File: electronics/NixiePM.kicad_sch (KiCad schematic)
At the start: 15 parts, among them U1 IRM-03-5, U2 16A 20mm 500V 5mm Plugin Fuse, U3 ESP32-ZERO, U4 QNHC3, U5 74HC595D,118, U6 74HC595D,118, U7 74HC595D,118, U8 KAQY214ATLD

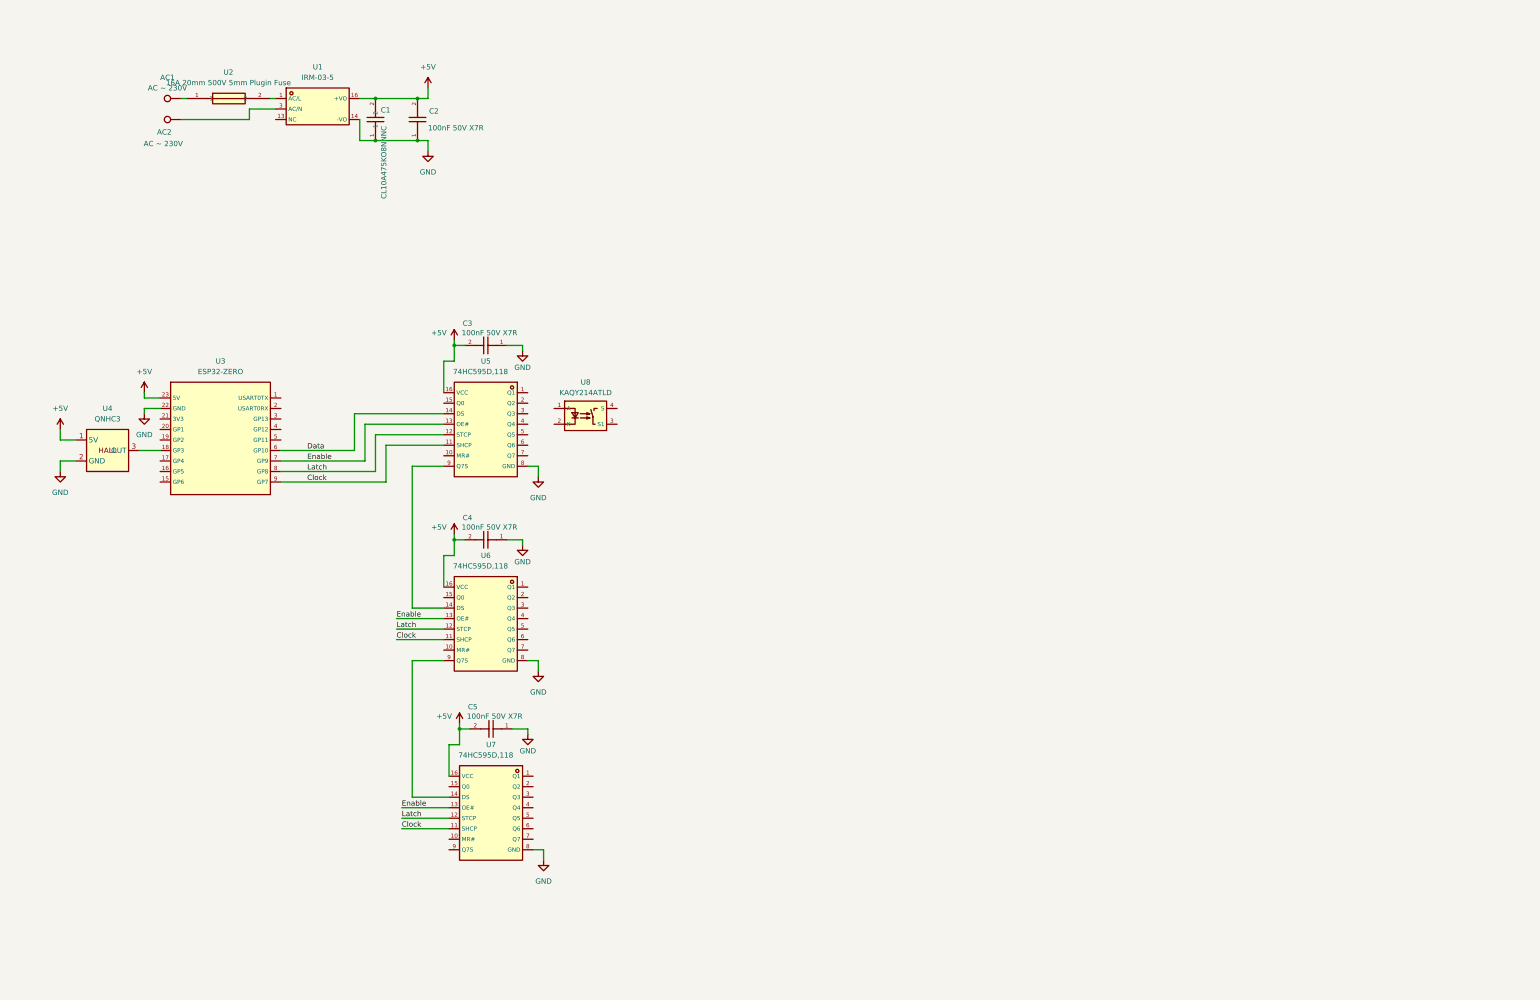
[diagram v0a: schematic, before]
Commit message: schematic ready, layout started
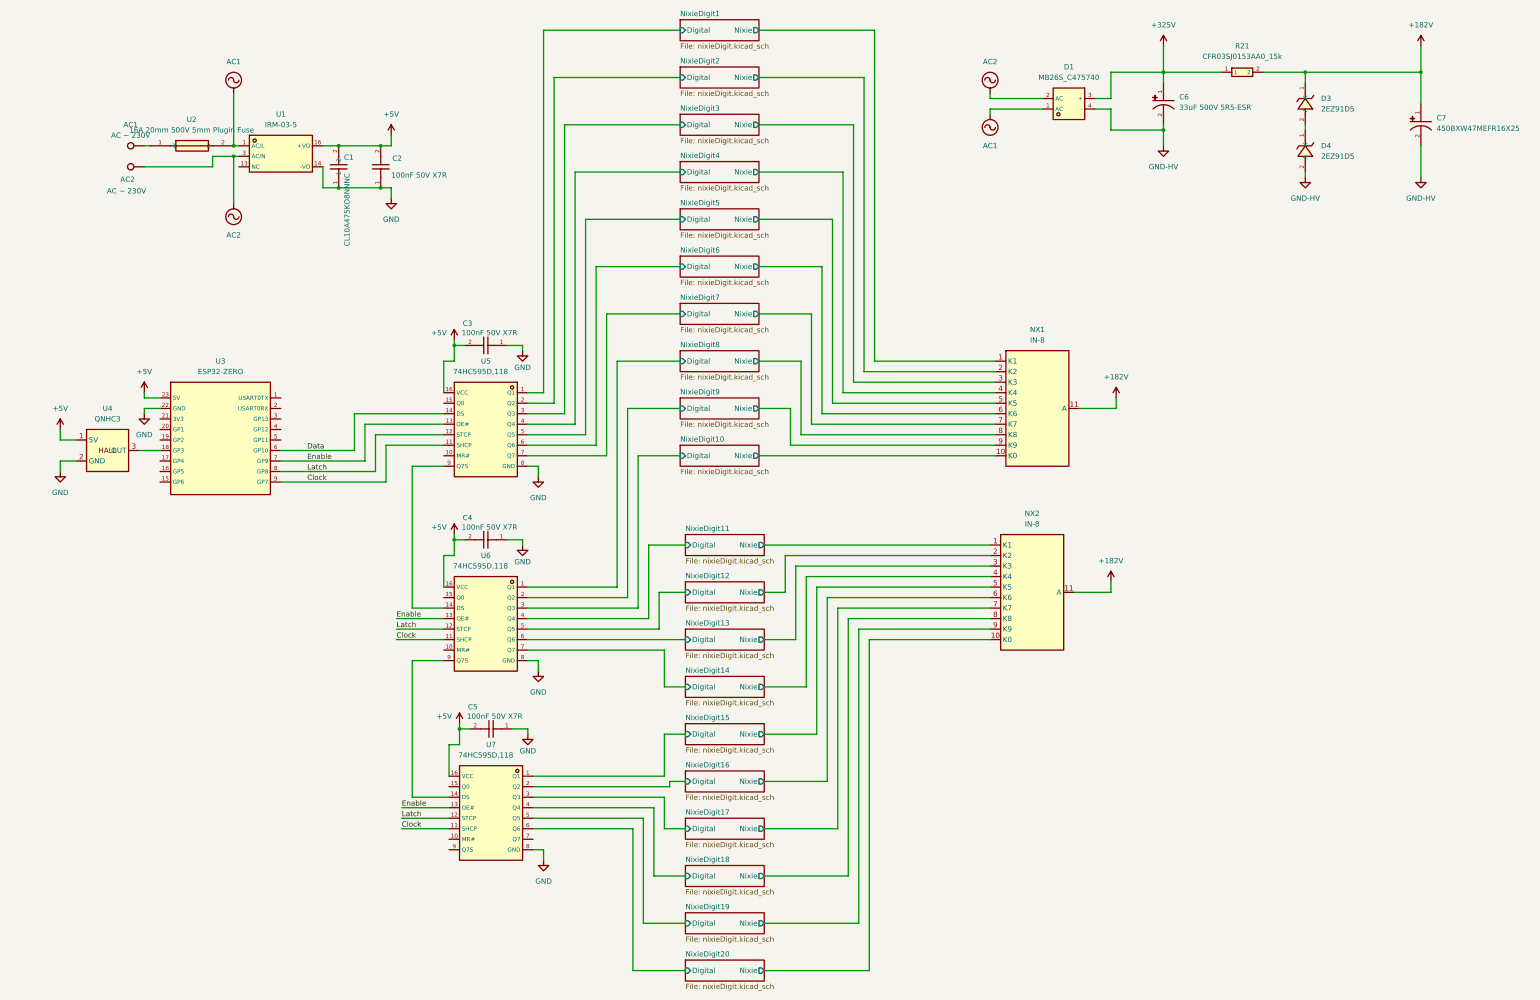
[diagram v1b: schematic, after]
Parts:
- removed U8: KAQY214ATLD, footprints:SMD-4_L4.6-W6.4-P2.54-LS10.0-BR, symbol symbols:KAQY214ATLD
- added C6: 33uF 500V 5R5-ESR, footprints:CAP-TH_BD12.5-P5.00-D0.6-FD, symbol symbols:LKML2502H330MF
- added C7: 450BXW47MEFR16X25, footprints:CAP-TH_BD16.0-P7.50-D1.2-FD, symbol symbols:450BXW47MEFR16X25
- added D1: MB26S_C475740, footprints:MBS_L4.7-W4.0-P2.50-LS7.0-BL, symbol symbols:MB26S_C475740
- added D3, D4: 2EZ91D5, footprints:DO-41_BD2.4-L4.7-P8.70-D0.8-RD, symbol symbols:2EZ91D5
- added NX1, NX2: IN-8, footprints:IN-8_NIXIE, symbol symbols:IN-8
- added R21: CFR03SJ0153AA0_15k, footprints:RES-TH_BD6.0-L17.5-P21.50-D0.8, symbol symbols:CFR03SJ0153AA0
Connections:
- net NixieDigit1/Digital: now reaches U5.1 (Q1)
- net NixieDigit2/Digital: now reaches U5.2 (Q2)
- net NixieDigit3/Digital: now reaches U5.3 (Q3)
- net NixieDigit4/Digital: now reaches U5.4 (Q4)
- net NixieDigit5/Digital: now reaches U5.5 (Q5)
- net NixieDigit6/Digital: now reaches U5.6 (Q6)
- net NixieDigit7/Digital: now reaches U5.7 (Q7)
- net AC2: now reaches AC2.1, U1.3 (AC/N)
- net AC2: now also D1.2 (AC)
- net NixieDigit8/Digital: now reaches U6.1 (Q1)
- net NixieDigit9/Digital: now reaches U6.2 (Q2)
- net NixieDigit10/Digital: now reaches U6.3 (Q3)
- net NixieDigit11/Digital: now reaches U6.4 (Q4)
- net NixieDigit12/Digital: now reaches U6.5 (Q5)
- net NixieDigit13/Digital: now reaches U6.6 (Q6)
- net NixieDigit14/Digital: now reaches U6.7 (Q7)
- net AC1: now reaches U1.1 (AC/L), U2.2
- net AC1: now also D1.1 (AC)
- net NixieDigit15/Digital: now reaches U7.1 (Q1)
- net NixieDigit16/Digital: now reaches U7.2 (Q2)
- net NixieDigit17/Digital: now reaches U7.3 (Q3)
- net NixieDigit18/Digital: now reaches U7.4 (Q4)
- net NixieDigit19/Digital: now reaches U7.5 (Q5)
- net NixieDigit20/Digital: now reaches U7.6 (Q6)
- new net: D3.2 (A), D4.1 (K)
- new net +182V: C7.1, D3.1 (K), NX1.11 (A), NX2.11 (A), R21.2
- new net +325V: C6.1, D1.3 (+), R21.1
- new net GND-HV: C6.2, C7.2, D1.4 (-), D4.2 (A)
- new net NixieDigit1/Nixie: NX1.1 (K1)
- new net NixieDigit10/Nixie: NX1.10 (K0)
- new net NixieDigit11/Nixie: NX2.1 (K1)
- new net NixieDigit12/Nixie: NX2.2 (K2)
- new net NixieDigit13/Nixie: NX2.3 (K3)
- new net NixieDigit14/Nixie: NX2.4 (K4)
- new net NixieDigit15/Nixie: NX2.5 (K5)
- new net NixieDigit16/Nixie: NX2.6 (K6)
- new net NixieDigit17/Nixie: NX2.7 (K7)
- new net NixieDigit18/Nixie: NX2.8 (K8)
- new net NixieDigit19/Nixie: NX2.9 (K9)
- new net NixieDigit2/Nixie: NX1.2 (K2)
- new net NixieDigit20/Nixie: NX2.10 (K0)
- new net NixieDigit3/Nixie: NX1.3 (K3)
- new net NixieDigit4/Nixie: NX1.4 (K4)
- new net NixieDigit5/Nixie: NX1.5 (K5)
- new net NixieDigit6/Nixie: NX1.6 (K6)
- new net NixieDigit7/Nixie: NX1.7 (K7)
- new net NixieDigit8/Nixie: NX1.8 (K8)
- new net NixieDigit9/Nixie: NX1.9 (K9)
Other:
- added sheet NixieDigit1 (nixieDigit.kicad_sch)
- added sheet NixieDigit10 (nixieDigit.kicad_sch)
- added sheet NixieDigit11 (nixieDigit.kicad_sch)
- added sheet NixieDigit12 (nixieDigit.kicad_sch)
- added sheet NixieDigit13 (nixieDigit.kicad_sch)
- added sheet NixieDigit14 (nixieDigit.kicad_sch)
- added sheet NixieDigit15 (nixieDigit.kicad_sch)
- added sheet NixieDigit16 (nixieDigit.kicad_sch)
- added sheet NixieDigit17 (nixieDigit.kicad_sch)
- added sheet NixieDigit18 (nixieDigit.kicad_sch)
- added sheet NixieDigit19 (nixieDigit.kicad_sch)
- added sheet NixieDigit2 (nixieDigit.kicad_sch)
- added sheet NixieDigit20 (nixieDigit.kicad_sch)
- added sheet NixieDigit3 (nixieDigit.kicad_sch)
- added sheet NixieDigit4 (nixieDigit.kicad_sch)
- added sheet NixieDigit5 (nixieDigit.kicad_sch)
- added sheet NixieDigit6 (nixieDigit.kicad_sch)
- added sheet NixieDigit7 (nixieDigit.kicad_sch)
- added sheet NixieDigit8 (nixieDigit.kicad_sch)
- added sheet NixieDigit9 (nixieDigit.kicad_sch)
- moved on the sheet: AC1, AC2, C1, C2, U1, U2

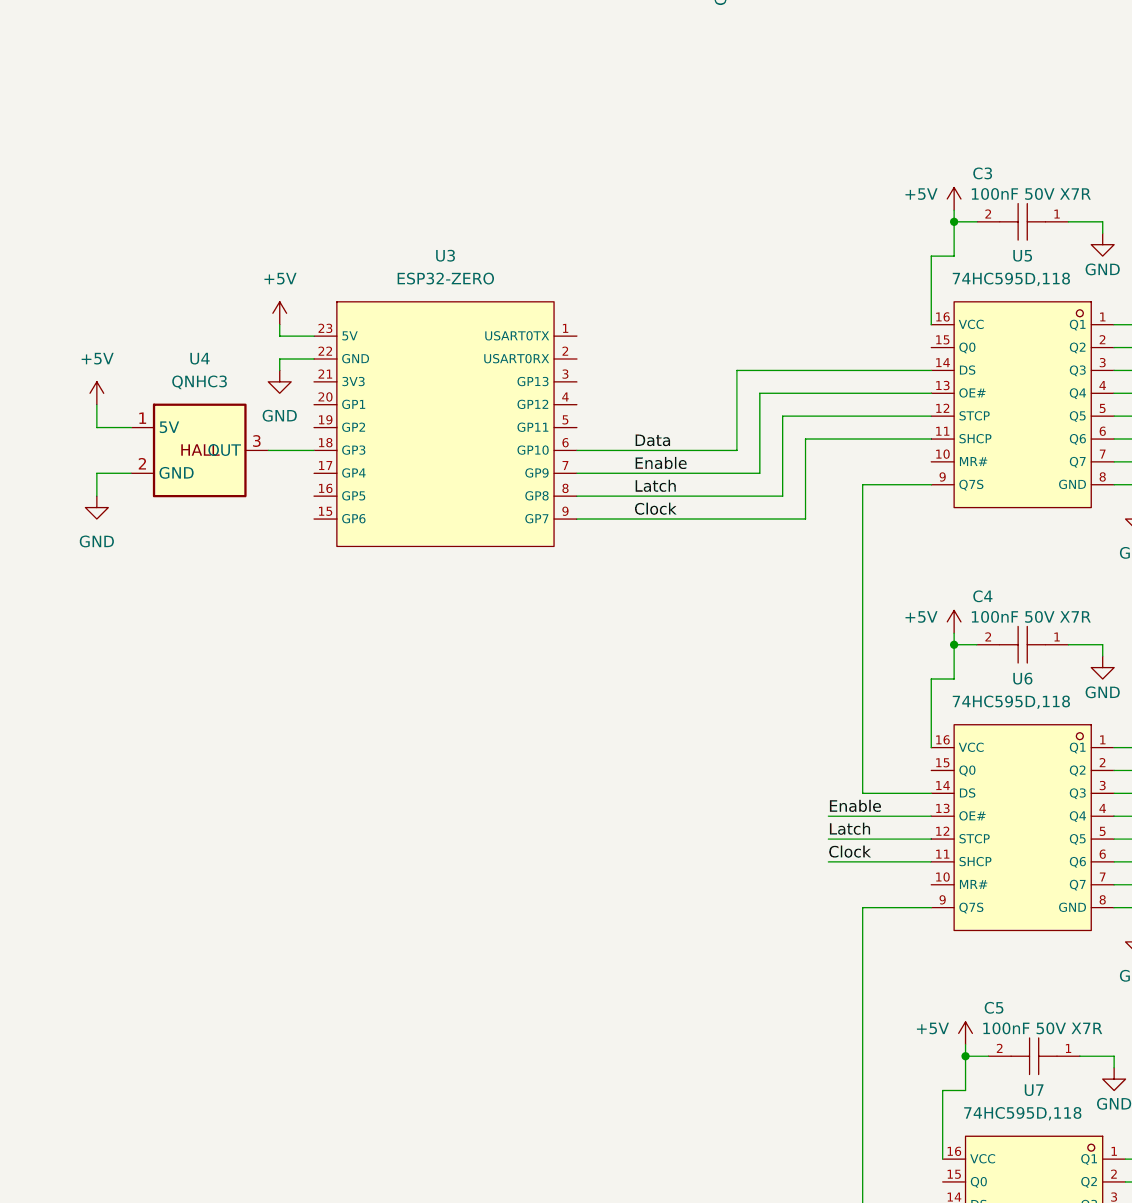
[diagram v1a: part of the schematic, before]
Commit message: update resistor, update voltages
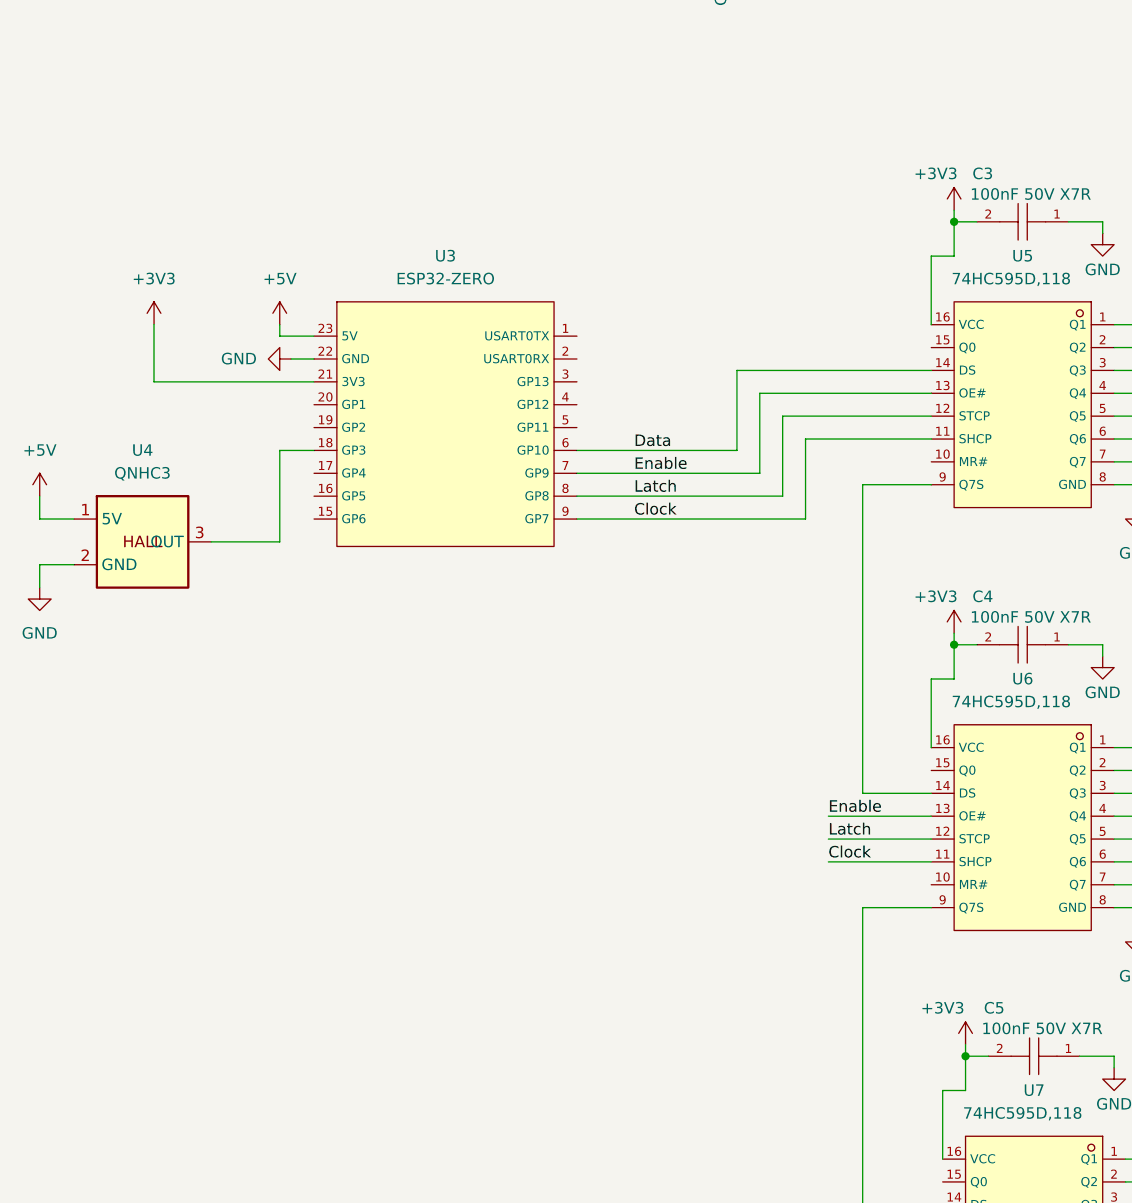
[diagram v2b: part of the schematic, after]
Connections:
- net +5V: no longer C3.2, C4.2, C5.2, U5.16 (VCC), U6.16 (VCC), U7.16 (VCC)
- net +3V3: now reaches U3.21 (3V3)
- net +3V3: now also C3.2, C4.2, C5.2, U5.16 (VCC), U6.16 (VCC), U7.16 (VCC)
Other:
- moved on the sheet: U4

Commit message: update schmatic
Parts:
- added C8: 0603B472K500NT, footprints:C0603, symbol symbols:0603B472K500NT
- added R22, R23: 0603WAF1002T5E, footprints:R0603, symbol symbols:0603WAF1002T5E
- added R24: 0603WAF1201T5E, footprints:R0603, symbol symbols:0603WAF1201T5E
- added R25: 0603WAF3301T5E, footprints:R0603, symbol symbols:0603WAF3301T5E
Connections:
- net +182V: now also R22.2, R23.2; no longer NX1.11 (A), NX2.11 (A)
- net GND: now also C8.1, R25.1
- net at U4.3 (OUT): now also R24.2; no longer U3.18 (GP3)
- net at U3.15 (GP6): now also C8.2, R24.1, R25.2
- new net Anode1: NX1.11 (A), R22.1
- new net Anode2: NX2.11 (A), R23.1
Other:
- note added: "47uF 450V"
- moved on the sheet: U4

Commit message: fix: schematic mistakes corrected
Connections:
- net Clock: now also U3.8 (GP8); no longer U3.9 (GP7)
- net Data: now also U3.5 (GP11); no longer U3.6 (GP10)
- net Enable: now also U3.6 (GP10); no longer U3.7 (GP9)
- net Latch: now also U3.7 (GP9); no longer U3.8 (GP8)
- net Reset: now reaches U5.10 (MR#)
- net Reset: now also U3.9 (GP7), U6.10 (MR#), U7.10 (MR#)
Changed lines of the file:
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@@
+	(wire
+		(pts
+			(xy 80.01 125.73) (xy 100.33 125.73)
+		)
+		(stroke
+			(width 0)
+			(type default)
+		)
+	)
 	(wire
 		(pts
@@
 	(wire
 		(pts
+			(xy 107.95 173.99) (xy 119.38 173.99)
+		)
+		(stroke
+			(width 0)
+			(type default)
+		)
+	)
+	(wire
+		(pts
 			(xy 64.77 163.83) (xy 64.77 167.64)
 		)
@@
 	(wire
 		(pts
-			(xy 80.01 125.73) (xy 97.79 125.73)
-		)
-		(stroke
-			(width 0)
-			(type default)
-		)
-	)
-	(wire
-		(pts
 			(xy 251.46 153.67) (xy 204.47 153.67)
 		)
@@
 	(wire
 		(pts
+			(xy 119.38 127) (xy 107.95 127)
+		)
+		(stroke
+			(width 0)
+			(type default)
+		)
+	)
+	(wire
+		(pts
 			(xy 140.97 212.09) (xy 170.18 212.09)
 		)
@@
 	(wire
 		(pts
-			(xy 100.33 128.27) (xy 80.01 128.27)
-		)
-		(stroke
-			(width 0)
-			(type default)
-		)
-	)
-	(wire
-		(pts
 			(xy 251.46 161.29) (xy 212.09 161.29)
 		)
@@
 	(wire
 		(pts
+			(xy 109.22 219.71) (xy 120.65 219.71)
+		)
+		(stroke
+			(width 0)
+			(type default)
+		)
+	)
+	(wire
+		(pts
 			(xy 119.38 163.83) (xy 111.76 163.83)
 		)
@@
 	(wire
 		(pts
+			(xy 80.01 133.35) (xy 107.95 133.35)
+		)
+		(stroke
+			(width 0)
+			(type default)
+		)
+	)
+	(wire
+		(pts
 			(xy 119.38 158.75) (xy 119.38 151.13)
 		)
@@
 	(wire
 		(pts
+			(xy 80.01 130.81) (xy 105.41 130.81)
+		)
+		(stroke
+			(width 0)
+			(type default)
+		)
+	)
+	(wire
+		(pts
 			(xy 176.53 81.28) (xy 156.21 81.28)
 		)
@@
 	(wire
 		(pts
+			(xy 107.95 127) (xy 107.95 133.35)
+		)
+		(stroke
+			(width 0)
+			(type default)
+		)
+	)
+	(wire
+		(pts
 			(xy 172.72 217.17) (xy 177.8 217.17)
 		)
@@
 	(wire
 		(pts
-			(xy 97.79 116.84) (xy 119.38 116.84)
+			(xy 99.06 116.84) (xy 119.38 116.84)
 		)
 		(stroke
@@
 	(wire
 		(pts
-			(xy 100.33 119.38) (xy 100.33 128.27)
+			(xy 100.33 119.38) (xy 100.33 125.73)
 		)
 		(stroke
@@
 	(wire
 		(pts
+			(xy 80.01 128.27) (xy 102.87 128.27)
+		)
+		(stroke
+			(width 0)
+			(type default)
+		)
+	)
+	(wire
+		(pts
+			(xy 80.01 123.19) (xy 99.06 123.19)
+		)
+		(stroke
+			(width 0)
+			(type default)
+		)
+	)
+	(wire
+		(pts
 			(xy 121.92 147.32) (xy 124.46 147.32)
 		)
@@
 	(wire
 		(pts
-			(xy 105.41 124.46) (xy 105.41 133.35)
+			(xy 105.41 124.46) (xy 105.41 130.81)
 		)
 		(stroke
@@
 	(wire
 		(pts
-			(xy 97.79 125.73) (xy 97.79 116.84)
+			(xy 99.06 123.19) (xy 99.06 116.84)
 		)
 		(stroke
@@
 	(wire
 		(pts
-			(xy 102.87 121.92) (xy 102.87 130.81)
+			(xy 102.87 121.92) (xy 102.87 128.27)
 		)
 		(stroke
@@
 	(wire
 		(pts
-			(xy 105.41 133.35) (xy 80.01 133.35)
-		)
-		(stroke
-			(width 0)
-			(type default)
-		)
-	)
-	(wire
-		(pts
 			(xy 143.51 111.76) (xy 143.51 24.13)
 		)
@@
 	(wire
 		(pts
-			(xy 102.87 130.81) (xy 80.01 130.81)
-		)
-		(stroke
-			(width 0)
-			(type default)
-		)
-	)
-	(wire
-		(pts
 			(xy 33.02 118.11) (xy 33.02 111.76)
 		)
@@
 	)
 	(label "Data"
-		(at 86.36 125.73 0)
+		(at 86.36 123.19 0)
+		(effects
+			(font
+				(size 1.27 1.27)
+			)
+			(justify left bottom)
+		)
+	)
+	(label "Reset"
+		(at 108.0997 173.99 0)
 		(effects
 			(font
@@
 	)
 	(label "Latch"
-		(at 86.36 130.81 0)
+		(at 86.36 128.27 0)
 		(effects
 			(font
@@
 		)
 	)
+	(label "Reset"
+		(at 109.3697 219.71 0)
+		(effects
+			(font
+				(size 1.27 1.27)
+			)
+			(justify left bottom)
+		)
+	)
 	(label "Anode1"
 		(at 276.86 115.57 0)
@@
 	)
 	(label "Clock"
+		(at 86.36 130.81 0)
+		(effects
+			(font
+				(size 1.27 1.27)
+			)
+			(justify left bottom)
+		)
+	)
+	(label "Reset"
 		(at 86.36 133.35 0)
 		(effects
@@
 	)
 	(label "Enable"
-		(at 86.36 128.27 0)
+		(at 86.36 125.73 0)
 		(effects
 			(font
